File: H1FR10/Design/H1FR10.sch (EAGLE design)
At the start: 22 parts, among them J1 U.FL-R-SMT-1_10_, P1 HEXABIT_17.32_NO_P6_P7_P12, U1 STM32G0B1CEU6N, U2 LORA127X-C1, X1 XTALL_CSTCE8M00G52

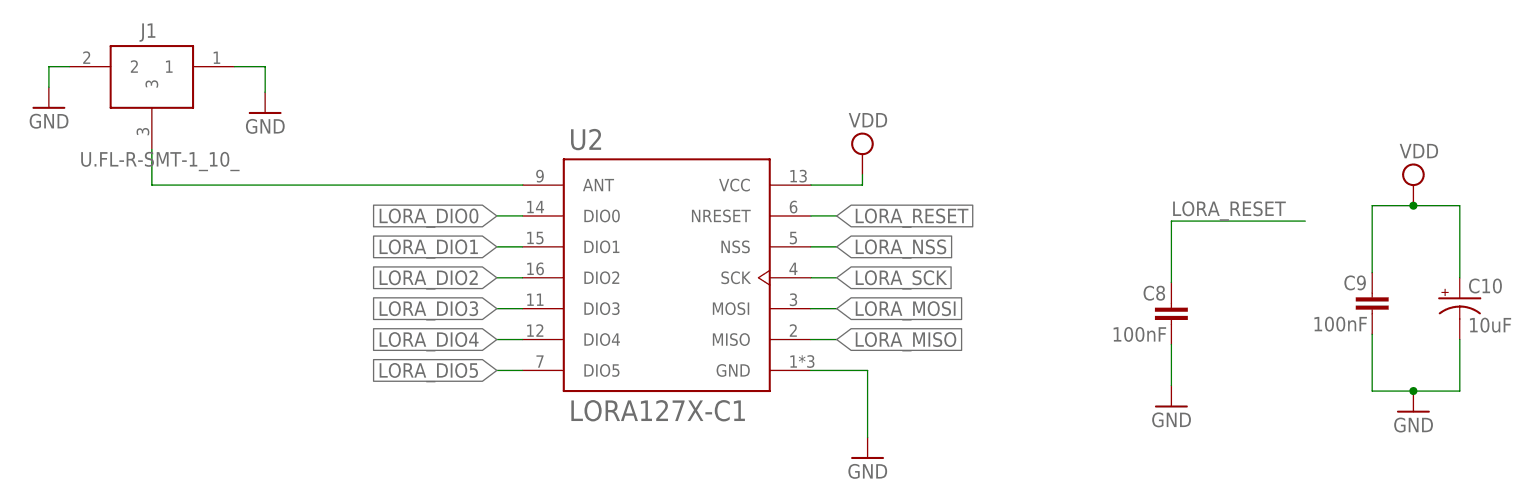
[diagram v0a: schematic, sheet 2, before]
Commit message: -Correct some documentaion issues
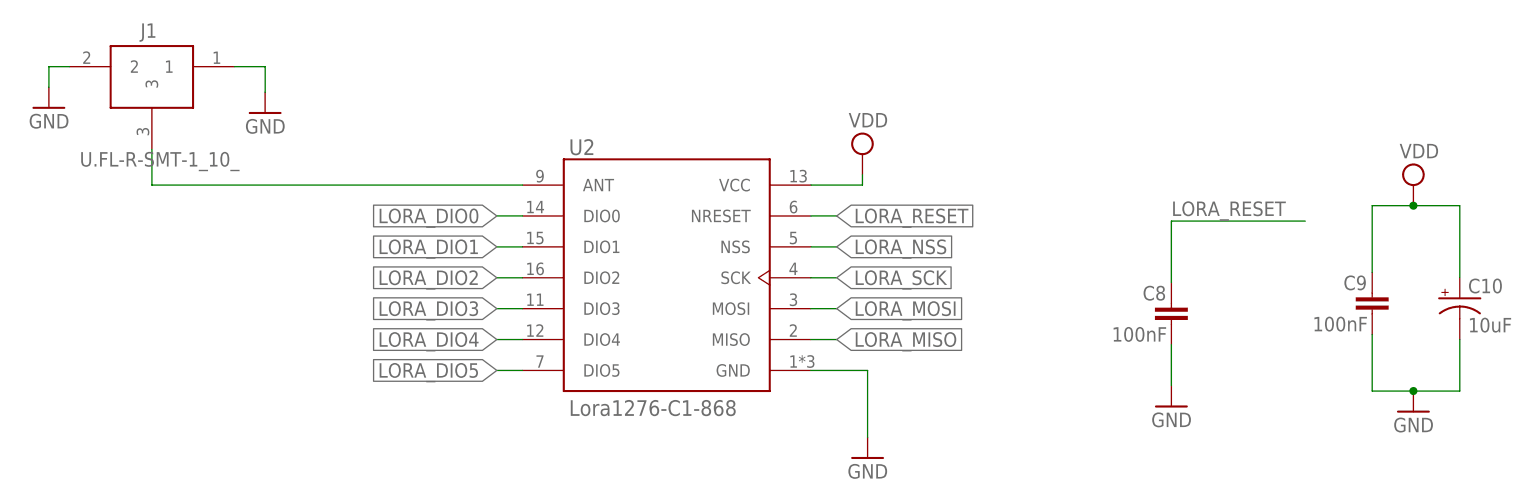
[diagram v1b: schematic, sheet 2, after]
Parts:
- U2: value LORA127X-C1 -> Lora1276-C1-868
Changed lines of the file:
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@@
 <part name="SWD" library="HEXABITZ_CONNECTION_PARTS" library_urn="urn:adsk.eagle:library:20064553" deviceset="PINHD-1X3" device="SWD" package3d_urn="urn:adsk.eagle:package:42172676/2"/>
 <part name="P1" library="hexabitz_connectors" library_urn="urn:adsk.eagle:library:20064578" deviceset="HEXABIT_?_NO_P6_P7_P12" device="17.32" package3d_urn="urn:adsk.eagle:package:20064634/2"/>
-<part name="U2" library="HEXABITZ_ICs" library_urn="urn:adsk.eagle:library:20064554" deviceset="LORA127X-C1" device="" package3d_urn="urn:adsk.eagle:package:42421660/4"/>
+<part name="U2" library="HEXABITZ_ICs" library_urn="urn:adsk.eagle:library:20064554" deviceset="LORA127X-C1" device="" package3d_urn="urn:adsk.eagle:package:42421660/4" value="Lora1276-C1-868"/>
 <part name="J1" library="HEXABITZ_CONNECTION_PARTS" library_urn="urn:adsk.eagle:library:20064553" deviceset="U.FL-R-SMT-1_10_" device="" package3d_urn="urn:adsk.eagle:package:42403633/2"/>
 <part name="GND3" library="supply1" library_urn="urn:adsk.eagle:library:371" deviceset="GND" device=""/>
@@
 <instances>
 <instance part="U2" gate="G$1" x="140.335" y="106.045" smashed="yes">
-<attribute name="NAME" x="128.2539" y="122.4512" size="2.54323125" layer="95"/>
-<attribute name="VALUE" x="128.2616" y="89.0115" size="2.541690625" layer="96"/>
+<attribute name="NAME" x="128.2539" y="121.8162" size="1.9304" layer="95"/>
+<attribute name="VALUE" x="128.2616" y="89.6465" size="1.9304" layer="96"/>
 </instance>
 <instance part="J1" gate="G$1" x="86.995" y="132.715" smashed="yes" rot="R180">
